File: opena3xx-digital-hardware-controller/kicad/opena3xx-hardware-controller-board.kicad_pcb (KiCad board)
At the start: 2 copper layers, 156.3 x 80.6 mm, 52 parts, among them J1 Conn_02x01, J2 Conn_02x01, J3 Conn_02x01, J4 Conn_02x01, J5 Raspberry_Pi_Zero, SW1 SW_MEC_5E, U1 MCP23017_SO, U2 MCP23017_SO, U3 MCP23017_SO, U4 MCP23017_SO, U5 MCP23017_SO, U6 MCP23017_SO, U7 MCP23017_SO, U8 MCP23017_SO

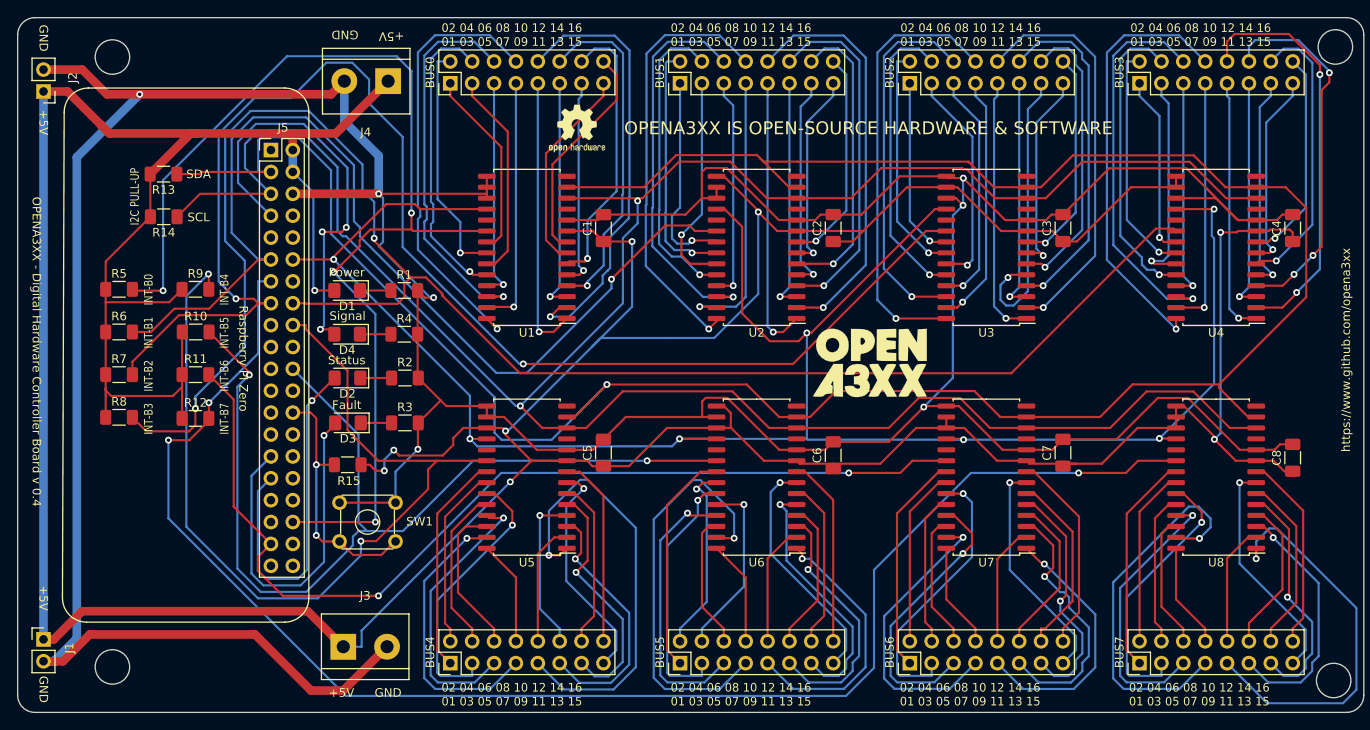
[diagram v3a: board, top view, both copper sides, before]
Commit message: Fixed Silkscreen for the BUS connectors - from 1/16 to 0/15
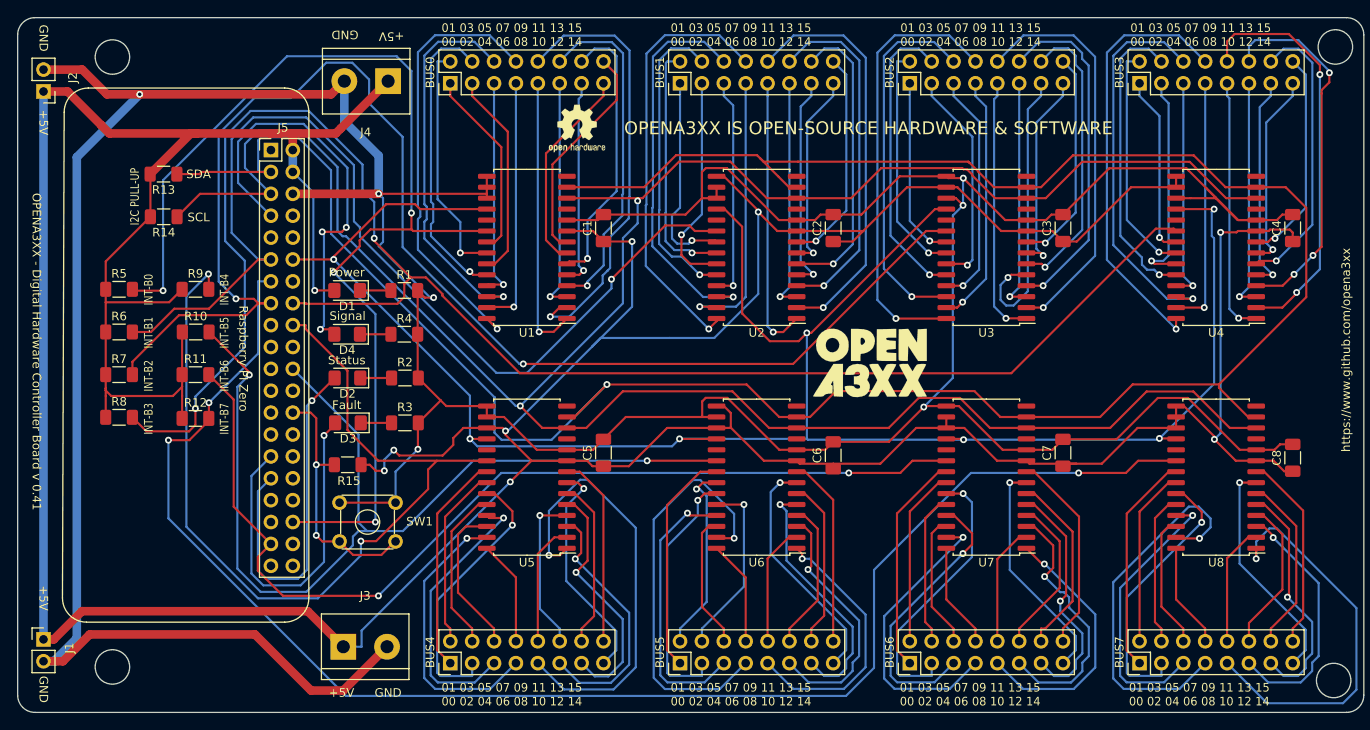
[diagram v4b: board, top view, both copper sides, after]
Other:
- board text added: "01 03 05 07 09 11 13 15 00 02 04 06 08 10 12 14"
- board text added: "OPENA3XX - Digital Hardware Controller Board v 0.41"
- board text removed: "02 04 06 08 10 12 14 16 01 03 05 07 09 11 13 15"
- board text removed: "OPENA3XX - Digital Hardware Controller Board v 0.4"

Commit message: Updated PCB MCDU v0.1
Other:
- board text added: "02 04 06 08 10 12 14 16 01 03 05 07 09 11 13 15"
- board text added: "OPENA3XX - Digital Hardware Controller Board v 0.4"
- board text removed: "01 03 05 07 09 11 13 15 00 02 04 06 08 10 12 14"
- board text removed: "OPENA3XX - Digital Hardware Controller Board v 0.41"
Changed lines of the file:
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@@
-(kicad_pcb (version 20171130) (host pcbnew 5.1.10-88a1d61d58~88~ubuntu20.04.1)
+(kicad_pcb (version 20171130) (host pcbnew "(5.1.9)-1")
   (general
     (thickness 1.6)
-    (drawings 59)
+    (drawings 63)
     (tracks 1589)
     (zones 0)
@@
     )
   )
+  (dimension 3.302 (width 0.15) (layer Dwgs.User)
+    (gr_text "3.302 mm" (at 213.6013 71.12714) (layer Dwgs.User)
+      (effects (font (size 1 1) (thickness 0.15)))
+    )
+    (feature1 (pts (xy 211.9503 65.69964) (xy 211.9503 70.413561)))
+    (feature2 (pts (xy 215.2523 65.69964) (xy 215.2523 70.413561)))
+    (crossbar (pts (xy 215.2523 69.82714) (xy 211.9503 69.82714)))
+    (arrow1a (pts (xy 211.9503 69.82714) (xy 213.076804 69.240719)))
+    (arrow1b (pts (xy 211.9503 69.82714) (xy 213.076804 70.413561)))
+    (arrow2a (pts (xy 215.2523 69.82714) (xy 214.125796 69.240719)))
+    (arrow2b (pts (xy 215.2523 69.82714) (xy 214.125796 70.413561)))
+  )
+  (dimension 3.556 (width 0.15) (layer Dwgs.User)
+    (gr_text "3.556 mm" (at 213.4743 149.67664) (layer Dwgs.User)
+      (effects (font (size 1 1) (thickness 0.15)))
+    )
+    (feature1 (pts (xy 211.6963 138.97864) (xy 211.6963 148.963061)))
+    (feature2 (pts (xy 215.2523 138.97864) (xy 215.2523 148.963061)))
+    (crossbar (pts (xy 215.2523 148.37664) (xy 211.6963 148.37664)))
+    (arrow1a (pts (xy 211.6963 148.37664) (xy 212.822804 147.790219)))
+    (arrow1b (pts (xy 211.6963 148.37664) (xy 212.822804 148.963061)))
+    (arrow2a (pts (xy 215.2523 148.37664) (xy 214.125796 147.790219)))
+    (arrow2b (pts (xy 215.2523 148.37664) (xy 214.125796 148.963061)))
+  )
+  (dimension 11.1125 (width 0.15) (layer Dwgs.User)
+    (gr_text "11.113 mm" (at 64.53505 145.54914) (layer Dwgs.User)
+      (effects (font (size 1 1) (thickness 0.15)))
+    )
+    (feature1 (pts (xy 70.0913 137.58164) (xy 70.0913 144.835561)))
+    (feature2 (pts (xy 58.9788 137.58164) (xy 58.9788 144.835561)))
+    (crossbar (pts (xy 58.9788 144.24914) (xy 70.0913 144.24914)))
+    (arrow1a (pts (xy 70.0913 144.24914) (xy 68.964796 144.835561)))
+    (arrow1b (pts (xy 70.0913 144.24914) (xy 68.964796 143.662719)))
+    (arrow2a (pts (xy 58.9788 144.24914) (xy 60.105304 144.835561)))
+    (arrow2b (pts (xy 58.9788 144.24914) (xy 60.105304 143.662719)))
+  )
+  (dimension 10.9855 (width 0.15) (layer Dwgs.User)
+    (gr_text "10.986 mm" (at 64.47155 61.72914) (layer Dwgs.User)
+      (effects (font (size 1 1) (thickness 0.15)))
+    )
+    (feature1 (pts (xy 69.9643 60.17514) (xy 69.9643 61.015561)))
+    (feature2 (pts (xy 58.9788 60.17514) (xy 58.9788 61.015561)))
+    (crossbar (pts (xy 58.9788 60.42914) (xy 69.9643 60.42914)))
+    (arrow1a (pts (xy 69.9643 60.42914) (xy 68.837796 61.015561)))
+    (arrow1b (pts (xy 69.9643 60.42914) (xy 68.837796 59.842719)))
+    (arrow2a (pts (xy 58.9788 60.42914) (xy 60.105304 61.015561)))
+    (arrow2b (pts (xy 58.9788 60.42914) (xy 60.105304 59.842719)))
+  )
   (dimension 4 (width 0.15) (layer Dwgs.User)
     (gr_text "4.000 mm" (at 70 57.12) (layer Dwgs.User)
@@
     (effects (font (size 1 0.8) (thickness 0.15)))
   )
-  (gr_text "OPENA3XX - Digital Hardware Controller Board v 0.41" (at 61.2 101 -90) (layer F.SilkS)
+  (gr_text "OPENA3XX - Digital Hardware Controller Board v 0.4" (at 61.2 101 270) (layer F.SilkS)
     (effects (font (size 1 1) (thickness 0.15)))
   )
@@
     (effects (font (size 1 1) (thickness 0.15)))
   )
-  (gr_text "01 03 05 07 09 11 13 15\n00 02 04 06 08 10 12 14" (at 108.2 64.23) (layer F.SilkS)
+  (gr_text "02 04 06 08 10 12 14 16\n01 03 05 07 09 11 13 15" (at 108.2 64.23) (layer F.SilkS)
     (effects (font (size 1 0.96) (thickness 0.15)) (justify left))
   )
-  (gr_text "01 03 05 07 09 11 13 15\n00 02 04 06 08 10 12 14" (at 134.8 64.23) (layer F.SilkS)
+  (gr_text "02 04 06 08 10 12 14 16\n01 03 05 07 09 11 13 15" (at 134.8 64.23) (layer F.SilkS)
     (effects (font (size 1 0.96) (thickness 0.15)) (justify left))
   )
-  (gr_text "01 03 05 07 09 11 13 15\n00 02 04 06 08 10 12 14" (at 161.465 64.23) (layer F.SilkS)
+  (gr_text "02 04 06 08 10 12 14 16\n01 03 05 07 09 11 13 15" (at 161.465 64.23) (layer F.SilkS)
     (effects (font (size 1 0.96) (thickness 0.15)) (justify left))
   )
-  (gr_text "01 03 05 07 09 11 13 15\n00 02 04 06 08 10 12 14" (at 188.165 64.23) (layer F.SilkS)
+  (gr_text "02 04 06 08 10 12 14 16\n01 03 05 07 09 11 13 15" (at 188.165 64.23) (layer F.SilkS)
     (effects (font (size 1 0.96) (thickness 0.15)) (justify left))
   )
-  (gr_text "01 03 05 07 09 11 13 15\n00 02 04 06 08 10 12 14" (at 188 140.8) (layer F.SilkS)
+  (gr_text "02 04 06 08 10 12 14 16\n01 03 05 07 09 11 13 15" (at 188 140.8) (layer F.SilkS)
     (effects (font (size 1 0.96) (thickness 0.15)) (justify left))
   )
-  (gr_text "01 03 05 07 09 11 13 15\n00 02 04 06 08 10 12 14" (at 161.4 140.8) (layer F.SilkS)
+  (gr_text "02 04 06 08 10 12 14 16\n01 03 05 07 09 11 13 15" (at 161.4 140.8) (layer F.SilkS)
     (effects (font (size 1 0.96) (thickness 0.15)) (justify left))
   )
-  (gr_text "01 03 05 07 09 11 13 15\n00 02 04 06 08 10 12 14" (at 134.8 140.8) (layer F.SilkS)
+  (gr_text "02 04 06 08 10 12 14 16\n01 03 05 07 09 11 13 15" (at 134.8 140.8) (layer F.SilkS)
     (effects (font (size 1 0.96) (thickness 0.15)) (justify left))
   )
-  (gr_text "01 03 05 07 09 11 13 15\n00 02 04 06 08 10 12 14" (at 108.2 140.8) (layer F.SilkS)
+  (gr_text "02 04 06 08 10 12 14 16\n01 03 05 07 09 11 13 15" (at 108.2 140.8) (layer F.SilkS)
     (effects (font (size 1 0.96) (thickness 0.15)) (justify left))
   )
